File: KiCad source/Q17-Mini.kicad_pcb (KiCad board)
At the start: 2 copper layers, 95 x 75 mm, 85 parts, among them J1 Input, J2-1 SPK+, J2-2 SPK-, J3-1 V+, J3-2 GND, J3-3 V-, Q1 IRF610, Q10 KSA992, Q11 BS250P, Q12 BD139, Q13 IRF610, Q14 IRF9610, Q15 FQA46N15, Q16 FQA36P15, Q2 KSA992, Q3 KSC1845, Q4 IRF9610, Q5 FQP3P20, Q6 FQP3N30, Q7 KSC1845, Q8 ZVN4206AV, Q9 BS250P, U1 OPA1641, U1' OPA1641

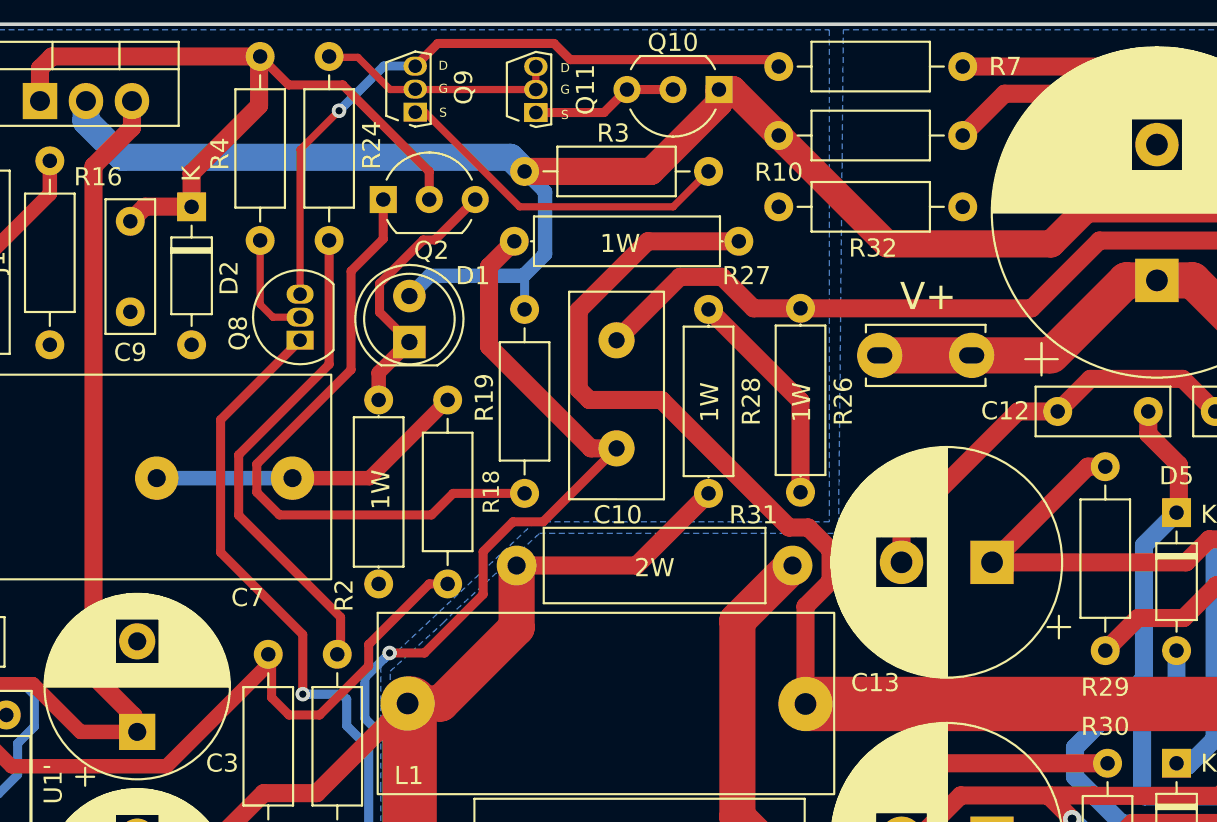
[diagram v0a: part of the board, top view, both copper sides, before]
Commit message: PCB 1.0.8
- Moved R27
- Moved C10
- New footprint for R27
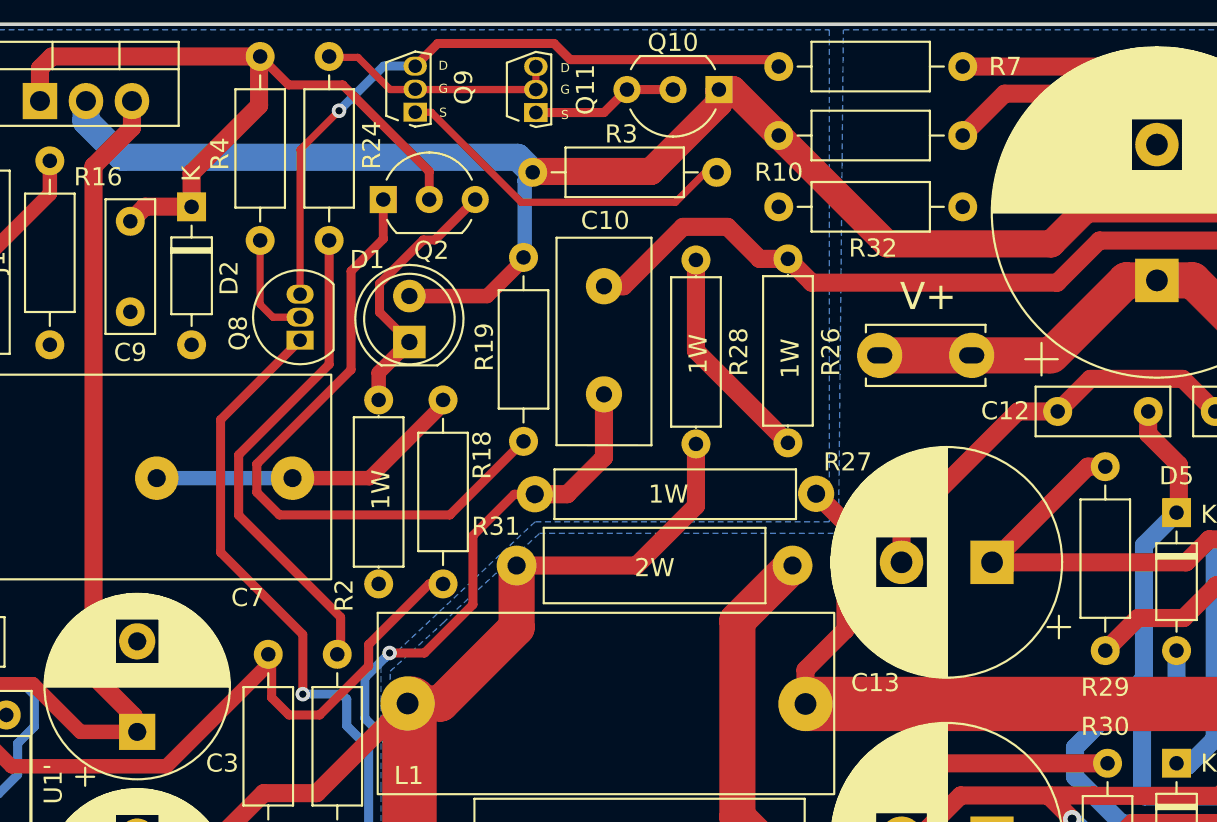
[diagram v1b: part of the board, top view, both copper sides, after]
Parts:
- moved R27 14.0 mm to (139.2, 81.0)
- moved C10 3.06 mm to (143.0, 69.6)
- moved R19 2.87 mm to (138.6, 67.9)
- moved R26 2.82 mm to (153.2, 68.0)
- moved R28 2.82 mm to (148.1, 68.1)
- moved R3 0.45 mm to (139.1, 63.2)
- moved R18 0.25 mm to (134.1, 75.8)
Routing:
- net Net-(L1-Pad2): track 101.4 -> 73.2 mm
- net Net-(C10-Pad2): track 83.3 -> 71.0 mm
- net Net-(C11-Pad2): track 160.1 -> 156.9 mm
- net Net-(J2-1-Pad1): track 74.5 -> 77.0 mm
- net Net-(Q2-Pad1): track 34.9 -> 36.0 mm
- net Net-(C10-Pad1): track 106.9 -> 107.5 mm

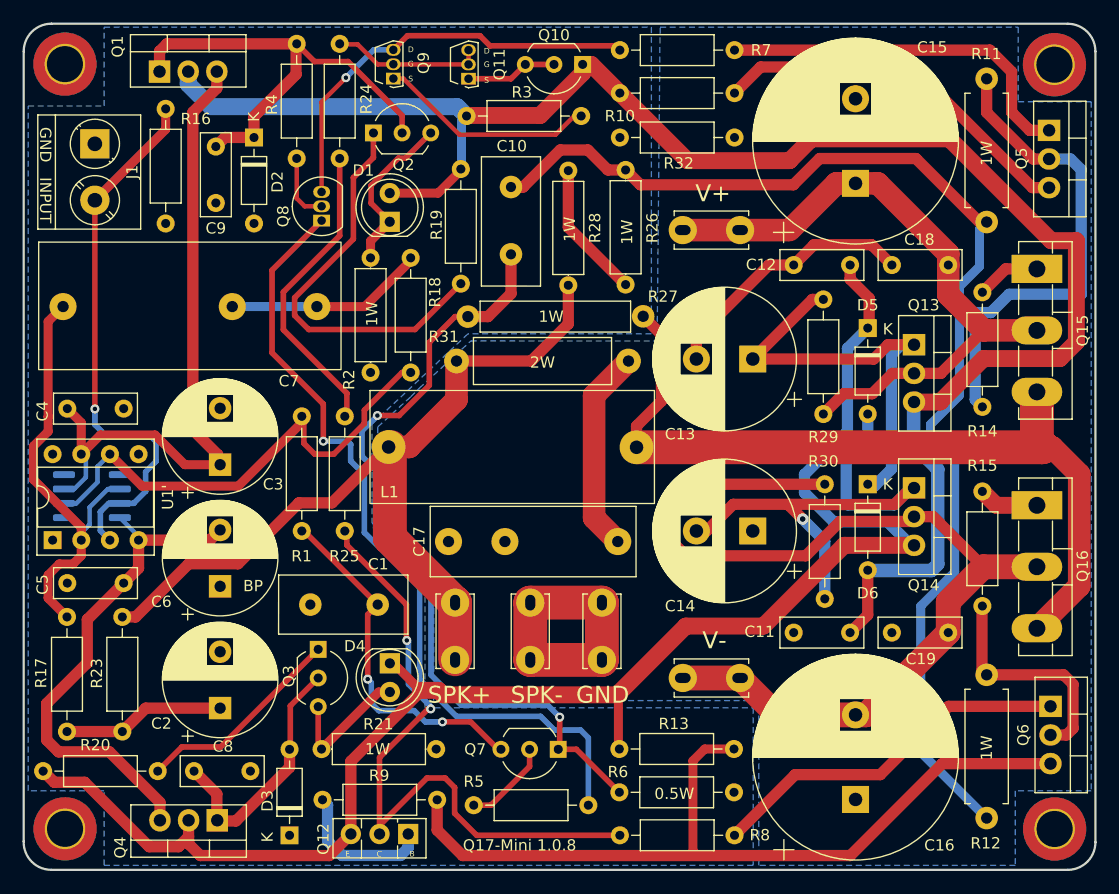
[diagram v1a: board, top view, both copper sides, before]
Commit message: PCB v1.0.8
Update some tracks.
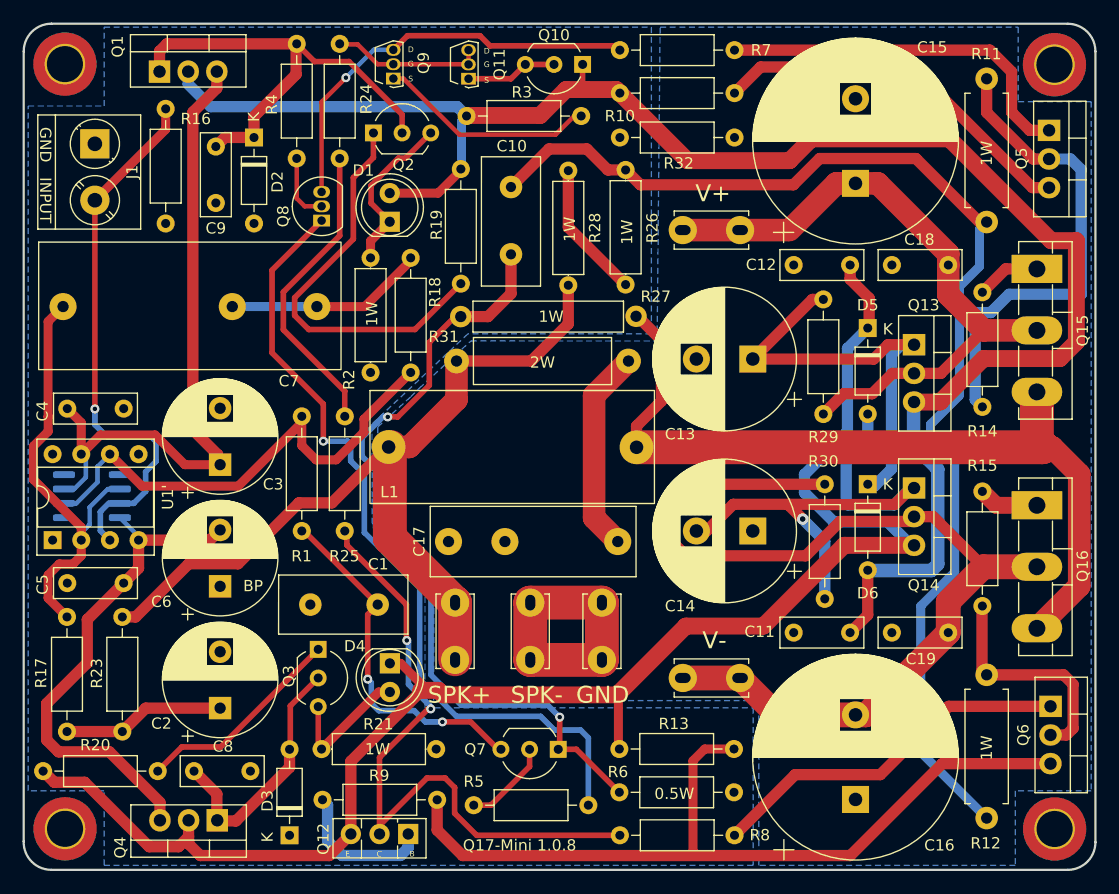
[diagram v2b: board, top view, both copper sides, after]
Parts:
- moved R27 0.63 mm to (138.5, 81.0)
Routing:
- net GNDPWR: track 46.2 -> 22.9 mm

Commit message: PCB v1.0.8
- New 3D model for L1
- Some tracks mods
- Some silkscreen mods.
- Removed tracks inside PAD.
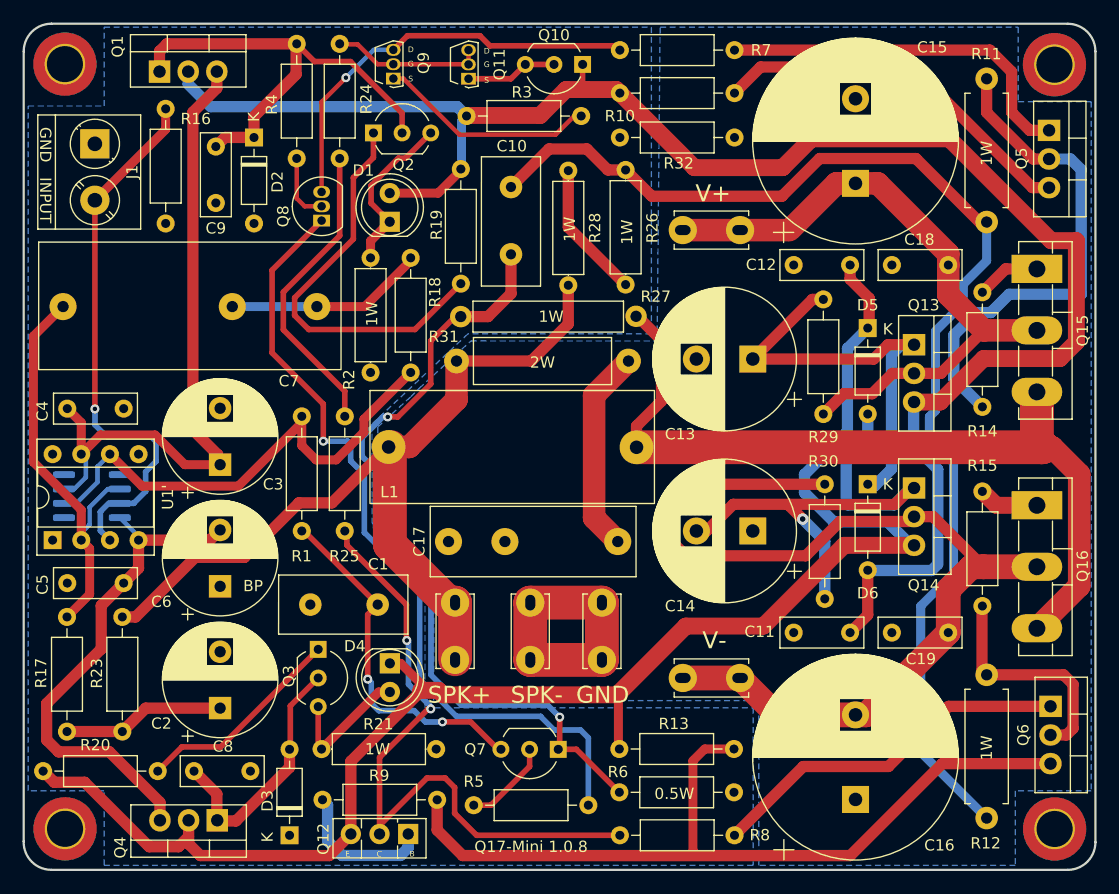
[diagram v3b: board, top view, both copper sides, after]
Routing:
- net Net-(Q5-Pad2): track 43.1 -> 44.7 mm
- net Net-(C7-Pad1): track 39.5 -> 38.1 mm
- net Net-(C12-Pad2): track 142.6 -> 141.7 mm
- net Net-(C10-Pad1): track 107.6 -> 108.4 mm
- net Net-(C16-Pad2): track 89.0 -> 89.6 mm
- net Net-(C3-Pad1): track 59.9 -> 59.3 mm
- net Net-(Q5-Pad3): track 33.3 -> 32.7 mm
- net Net-(C10-Pad2): track 70.6 -> 70.1 mm
- net Net-(Q8-Pad3): track 37.4 -> 36.8 mm
- net Net-(C14-Pad2): track 46.0 -> 45.4 mm

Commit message: pcB v1.0.8
- Move some tracks around Q15 and Q16.
- Move Faston connectors for more space.
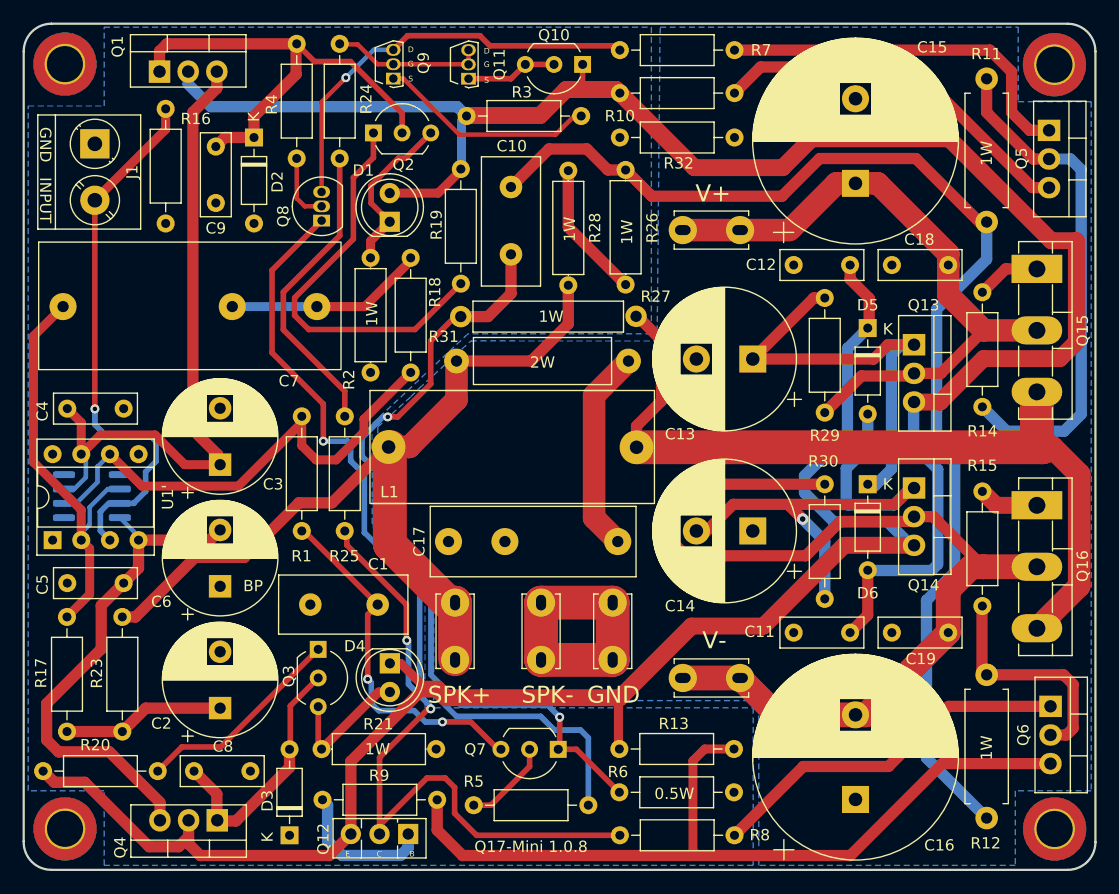
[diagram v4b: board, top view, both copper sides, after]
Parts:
- moved J2-2 0.96 mm to (145.7, 106.4)
- moved J3-2 0.96 mm to (152.0, 106.4)
- moved R29 0.18 mm to (170.8, 89.5)
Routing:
- net Net-(C10-Pad1): track 108.4 -> 107.6 mm
- net Net-(Q5-Pad2): track 44.7 -> 45.4 mm
- net Net-(C12-Pad2): track 141.7 -> 141.2 mm
- net Net-(C15-Pad1): track 59.1 -> 58.6 mm

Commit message: PCB v1.0.8
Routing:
- net Net-(C10-Pad1): track 107.6 -> 106.7 mm
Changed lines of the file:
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@@
     )
     (fp_line (start 9.2075 0) (end 9.275 0) (layer "F.SilkS") (width 0.12))
+    (fp_line (start 0.9525 1.3716) (end 9.2075 1.3716) (layer "F.SilkS") (width 0.12))
     (fp_line (start 9.2075 -1.3716) (end 0.9525 -1.3716) (layer "F.SilkS") (width 0.12))
     (fp_line (start 0.9525 -1.3716) (end 0.9525 1.3716) (layer "F.SilkS") (width 0.12))
     (fp_line (start 0.885 0) (end 0.9525 0) (layer "F.SilkS") (width 0.12))
-    (fp_line (start 0.9525 1.3716) (end 9.2075 1.3716) (layer "F.SilkS") (width 0.12))
     (fp_line (start 9.2075 1.3716) (end 9.2075 -1.3716) (layer "F.SilkS") (width 0.12))
     (fp_line (start -1.05 -1.5) (end -1.05 1.5) (layer "F.CrtYd") (width 0.05))
@@
   (segment (start 153.162 68.027373) (end 151.593373 68.027373) (width 1) (layer "F.Cu") (net 11))
   (segment (start 167.02002 70.358) (end 155.492627 70.358) (width 1) (layer "F.Cu") (net 11))
-  (segment (start 180.721 92.335737) (end 180.721 89.414293) (width 1) (layer "B.Cu") (net 11))
-  (segment (start 180.72952 89.405773) (end 180.72952 80.377586) (width 1) (layer "B.Cu") (net 11))
-  (segment (start 182.329031 103.674969) (end 182.329031 93.943769) (width 1) (layer "B.Cu") (net 11))
-  (segment (start 185.166 125.476) (end 179.832 120.142) (width 1) (layer "B.Cu") (net 11))
-  (segment (start 180.72952 80.377586) (end 185.166 75.941106) (width 1) (layer "B.Cu") (net 11))
   (segment (start 179.832 106.172) (end 182.329031 103.674969) (width 1) (layer "B.Cu") (net 11))
+  (segment (start 181.737 93.351738) (end 181.737 79.370106) (width 1) (layer "B.Cu") (net 11))
+  (segment (start 181.737 79.370106) (end 185.166 75.941106) (width 1) (layer "B.Cu") (net 11))
+  (segment (start 182.329031 93.943769) (end 181.737 93.351738) (width 1) (layer "B.Cu") (net 11))
   (segment (start 185.166 75.941106) (end 185.166 72.644) (width 1) (layer "B.Cu") (net 11))
-  (segment (start 180.721 89.414293) (end 180.72952 89.405773) (width 1) (layer "B.Cu") (net 11))
-  (segment (start 182.329031 93.943769) (end 180.721 92.335737) (width 1) (layer "B.Cu") (net 11))
+  (segment (start 182.329031 103.674969) (end 182.329031 93.943769) (width 1) (layer "B.Cu") (net 11))
   (segment (start 179.832 120.142) (end 179.832 106.172) (width 1) (layer "B.Cu") (net 11))
+  (segment (start 185.166 125.476) (end 179.832 120.142) (width 1) (layer "B.Cu") (net 11))
   (segment (start 190.883709 74.297709) (end 181.851969 65.265969) (width 1.5) (layer "F.Cu") (net 12))
   (segment (start 145.59078 63.19722) (end 147.8915 60.8965) (width 1.5) (layer "F.Cu") (net 12))

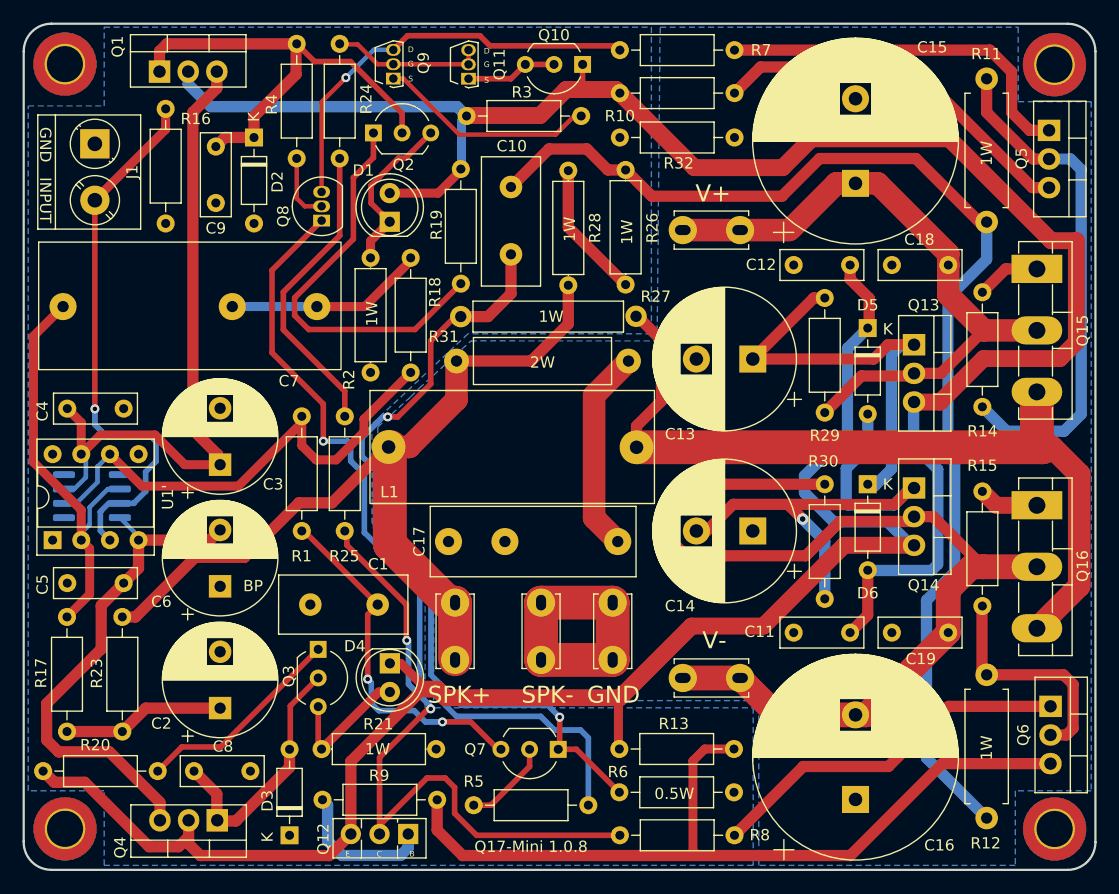
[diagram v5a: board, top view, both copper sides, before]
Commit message: PCB v1.0.8
Inversion des bornes SPK+ and GND.
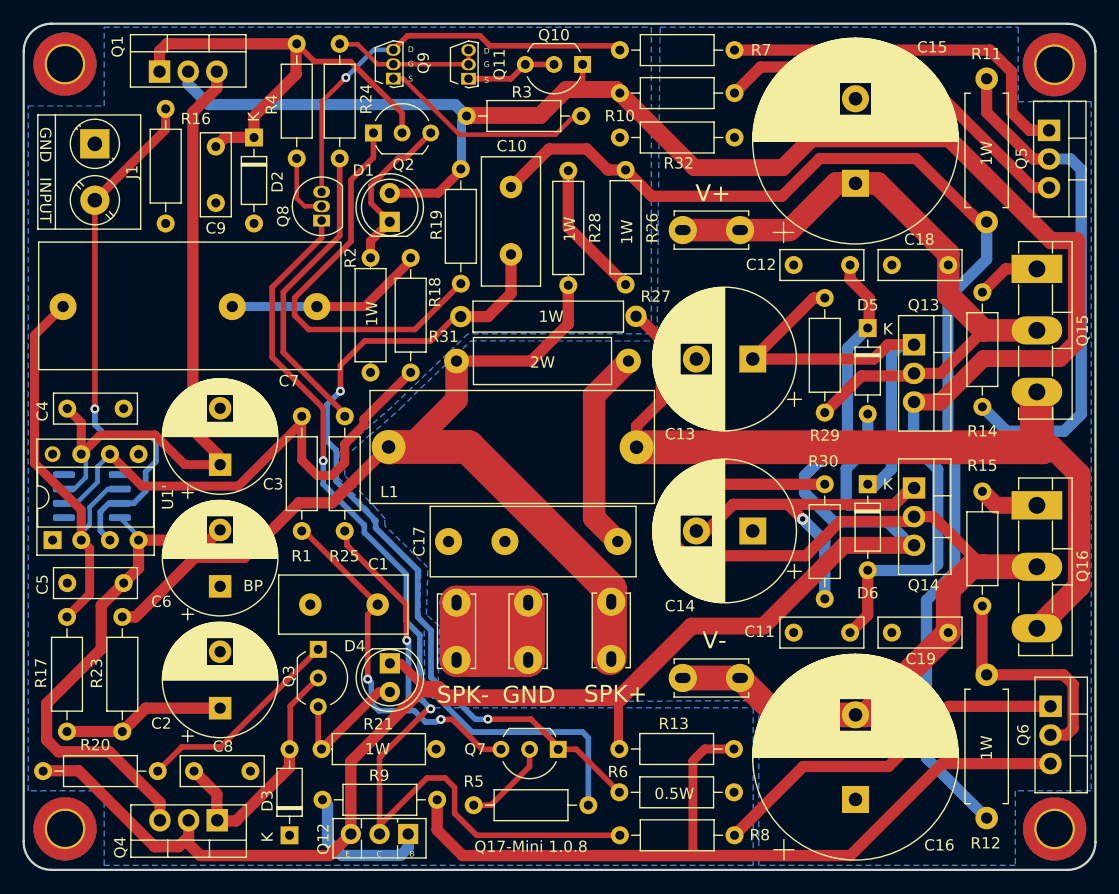
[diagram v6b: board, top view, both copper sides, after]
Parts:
- moved J2-1 13.8 mm to (151.9, 111.4)
- moved J2-2 7.49 mm to (138.2, 106.4)
- moved J3-2 7.49 mm to (144.5, 106.4)
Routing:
- net GNDPWR: track 22.9 -> 37.1 mm
- net Net-(J2-1-Pad1): track 77.1 -> 86.6 mm
- net Net-(C10-Pad2): track 70.1 -> 73.8 mm
- net Net-(R1-Pad1): track 43.8 -> 46.3 mm
- net Net-(Q8-Pad1): track 72.2 -> 71.4 mm
- net Net-(Q12-Pad2): track 58.4 -> 59.1 mm

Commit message: PCB V1.0.8
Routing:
- net Net-(C1-Pad1): track 31.6 -> 35.9 mm
- net Net-(C10-Pad2): track 73.8 -> 75.2 mm
- net Net-(Q8-Pad1): track 71.4 -> 72.4 mm
- net Net-(Q12-Pad2): track 59.1 -> 58.3 mm
